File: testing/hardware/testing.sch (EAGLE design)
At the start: 17 parts

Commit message: CAM files for PCB
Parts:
- J1: value (none) -> SPI_COMM
- X1: value (none) -> POWER
- X2: value (none) -> CAN_HI_LO
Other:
- note added: "CAN Bus Testing Module"
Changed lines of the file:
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@@
 </variantdefs>
 <classes>
-<class number="0" name="default" width="0.3048" drill="0.508">
+<class number="0" name="default" width="0.762" drill="0.508">
 <clearance class="0" value="0.3048"/>
+</class>
+<class number="1" name="power" width="1.27" drill="0.508">
+<clearance class="1" value="0.508"/>
 </class>
 </classes>
@@
 <part name="P+5" library="SparkFun" deviceset="VCC" device=""/>
 <part name="GND4" library="SparkFun" deviceset="GND" device=""/>
-<part name="X1" library="con-wago-500" deviceset="W237-102" device=""/>
-<part name="X2" library="con-wago-500" deviceset="W237-102" device=""/>
-<part name="J1" library="con-amp" deviceset="MTA05-156" device=""/>
-<part name="FRAME1" library="frames" library_urn="urn:adsk.eagle:library:229" deviceset="FRAME_A_L" device=""/>
+<part name="X1" library="con-wago-500" deviceset="W237-102" device="" value="POWER"/>
+<part name="X2" library="con-wago-500" deviceset="W237-102" device="" value="CAN_HI_LO"/>
+<part name="J1" library="con-amp" deviceset="MTA05-156" device="" value="SPI_COMM"/>
+<part name="FRAME1" library="frames" library_urn="urn:adsk.eagle:library:229" deviceset="FRAME_A_L" device="" value="frame"/>
 </parts>
 <sheets>
 <sheet>
 <plain>
+<text x="185.42" y="25.4" size="2.54" layer="94">CAN Bus Testing Module </text>
 </plain>
 <instances>
@@
 </instance>
 <instance part="X2" gate="-2" x="254" y="121.92" smashed="yes" rot="R180">
-<attribute name="VALUE" x="256.54" y="125.603" size="1.778" layer="96" rot="R180"/>
+<attribute name="VALUE" x="254" y="117.983" size="1.778" layer="96" rot="R180"/>
 <attribute name="NAME" x="254" y="121.031" size="1.778" layer="95"/>
 </instance>
@@
 </segment>
 </net>
-<net name="GND" class="0">
+<net name="GND" class="1">
 <segment>
 <pinref part="GND" gate="1" pin="GND"/>
@@
 <wire x1="81.28" y1="99.06" x2="71.12" y2="99.06" width="0.1524" layer="91"/>
 <wire x1="71.12" y1="99.06" x2="71.12" y2="96.52" width="0.1524" layer="91"/>
-<wire x1="20.32" y1="116.84" x2="22.86" y2="116.84" width="0.1524" layer="91"/>
-<wire x1="22.86" y1="116.84" x2="81.28" y2="116.84" width="0.1524" layer="91"/>
 <wire x1="81.28" y1="116.84" x2="81.28" y2="99.06" width="0.1524" layer="91"/>
 <junction x="81.28" y="99.06"/>
 <pinref part="X1" gate="-2" pin="KL"/>
+<wire x1="20.32" y1="116.84" x2="22.86" y2="116.84" width="0.1524" layer="91"/>
+<wire x1="22.86" y1="116.84" x2="81.28" y2="116.84" width="0.1524" layer="91"/>
 <junction x="22.86" y="116.84"/>
 </segment>
@@
 </segment>
 </net>
-<net name="VCC" class="0">
+<net name="VCC" class="1">
 <segment>
 <pinref part="R1" gate="G$1" pin="2"/>
@@
 </sheet>
 </sheets>
+<errors>
+</errors>
 </schematic>
 </drawing>

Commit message: test module updates
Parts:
- added LED4, LED5: (no value), adafruit:LED5MM
- added R7, R8: 220 Ω, adafruit:R-US_0204/7
- added X3: TEST_LED, con-wago-500:W237-102
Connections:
- net N$1 renamed RXCAN
- net N$10 renamed CS
- net N$11 renamed SCK
- net N$12 renamed CAN_H
- net N$14 renamed SI
- net N$15 renamed SO
- net N$17 renamed CAN_L
- net N$2 renamed TXCAN
- net N$7 renamed INT
- new net N$1: R7.2, X3-2.KL
- new net N$10: LED5.A, R8.1
- new net N$2: R8.2, X3-1.KL
- new net N$7: LED4.A, R7.1
- net GND: now also LED4.C, LED5.C
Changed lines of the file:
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@@
 <part name="J1" library="con-amp" deviceset="MTA05-156" device="" value="SPI_COMM"/>
 <part name="FRAME1" library="frames" library_urn="urn:adsk.eagle:library:229" deviceset="FRAME_A_L" device="" value="frame"/>
+<part name="LED4" library="adafruit" deviceset="LED" device="5MM"/>
+<part name="R7" library="adafruit" deviceset="R-US_" device="0204/7" value="220 Ω"/>
+<part name="LED5" library="adafruit" deviceset="LED" device="5MM"/>
+<part name="R8" library="adafruit" deviceset="R-US_" device="0204/7" value="220 Ω"/>
+<part name="GND5" library="SparkFun" deviceset="GND" device=""/>
+<part name="GND6" library="SparkFun" deviceset="GND" device=""/>
+<part name="X3" library="con-wago-500" deviceset="W237-102" device="" value="TEST_LED"/>
 </parts>
 <sheets>
@@
 <attribute name="DRAWING_NAME" x="185.42" y="19.05" size="2.54" layer="94"/>
 </instance>
+<instance part="LED4" gate="G$1" x="203.2" y="78.74" smashed="yes">
+<attribute name="NAME" x="206.756" y="74.168" size="1.778" layer="95" rot="R90"/>
+<attribute name="VALUE" x="208.915" y="74.168" size="1.778" layer="96" rot="R90"/>
+</instance>
+<instance part="R7" gate="G$1" x="203.2" y="91.44" smashed="yes" rot="R90">
+<attribute name="NAME" x="201.7014" y="87.63" size="1.778" layer="95" rot="R90"/>
+<attribute name="VALUE" x="206.502" y="87.63" size="1.778" layer="96" rot="R90"/>
+</instance>
+<instance part="LED5" gate="G$1" x="220.98" y="78.74" smashed="yes">
+<attribute name="NAME" x="224.536" y="74.168" size="1.778" layer="95" rot="R90"/>
+<attribute name="VALUE" x="226.695" y="74.168" size="1.778" layer="96" rot="R90"/>
+</instance>
+<instance part="R8" gate="G$1" x="220.98" y="91.44" smashed="yes" rot="R90">
+<attribute name="NAME" x="219.4814" y="87.63" size="1.778" layer="95" rot="R90"/>
+<attribute name="VALUE" x="224.282" y="87.63" size="1.778" layer="96" rot="R90"/>
+</instance>
+<instance part="GND5" gate="1" x="203.2" y="63.5" smashed="yes">
+<attribute name="VALUE" x="200.66" y="60.96" size="1.778" layer="96"/>
+</instance>
+<instance part="GND6" gate="1" x="220.98" y="63.5" smashed="yes">
+<attribute name="VALUE" x="218.44" y="60.96" size="1.778" layer="96"/>
+</instance>
+<instance part="X3" gate="-1" x="246.38" y="99.06" smashed="yes" rot="R180">
+<attribute name="NAME" x="246.38" y="98.171" size="1.778" layer="95"/>
+</instance>
+<instance part="X3" gate="-2" x="246.38" y="104.14" smashed="yes" rot="R180">
+<attribute name="VALUE" x="241.3" y="92.837" size="1.778" layer="96"/>
+<attribute name="NAME" x="246.38" y="103.251" size="1.778" layer="95"/>
+</instance>
 </instances>
 <busses>
 </busses>
 <nets>
-<net name="N$2" class="0">
+<net name="TXCAN" class="0">
 <segment>
 <pinref part="CAN_CONTRL" gate="A" pin="TXCAN"/>
@@
 </segment>
 </net>
-<net name="N$1" class="0">
+<net name="RXCAN" class="0">
 <segment>
 <pinref part="CAN_CONTRL" gate="A" pin="RXCAN"/>
@@
 <wire x1="162.56" y1="144.78" x2="157.48" y2="144.78" width="0.1524" layer="91"/>
 <wire x1="157.48" y1="144.78" x2="157.48" y2="139.7" width="0.1524" layer="91"/>
+</segment>
+<segment>
+<pinref part="LED4" gate="G$1" pin="C"/>
+<wire x1="203.2" y1="73.66" x2="203.2" y2="66.04" width="0.1524" layer="91"/>
+<pinref part="GND5" gate="1" pin="GND"/>
+</segment>
+<segment>
+<pinref part="LED5" gate="G$1" pin="C"/>
+<wire x1="220.98" y1="73.66" x2="220.98" y2="66.04" width="0.1524" layer="91"/>
+<pinref part="GND6" gate="1" pin="GND"/>
 </segment>
 </net>
@@
 </segment>
 </net>
-<net name="N$7" class="0">
+<net name="INT" class="0">
 <segment>
 <pinref part="LED1" gate="G$1" pin="C"/>
@@
 </segment>
 </net>
-<net name="N$12" class="0">
+<net name="CAN_H" class="0">
 <segment>
 <pinref part="CAN_TRANS" gate="A" pin="CANH"/>
@@
 </segment>
 </net>
-<net name="N$17" class="0">
+<net name="CAN_L" class="0">
 <segment>
 <wire x1="251.46" y1="132.08" x2="248.92" y2="132.08" width="0.1524" layer="91"/>
@@
 <junction x="248.92" y="132.08"/>
 <junction x="236.22" y="132.08"/>
-</segment>
-</net>
-<net name="N$11" class="0">
+<wire x1="251.46" y1="132.08" x2="248.92" y2="132.08" width="0.1524" layer="91"/>
+</segment>
+</net>
+<net name="SCK" class="0">
 <segment>
 <pinref part="CAN_CONTRL" gate="A" pin="SCK"/>
@@
 </segment>
 </net>
-<net name="N$14" class="0">
+<net name="SI" class="0">
 <segment>
 <pinref part="J1" gate="G$1" pin="2"/>
@@
 </segment>
 </net>
-<net name="N$15" class="0">
+<net name="SO" class="0">
 <segment>
 <pinref part="J1" gate="G$1" pin="3"/>
@@
 </segment>
 </net>
-<net name="N$10" class="0">
+<net name="CS" class="0">
 <segment>
 <pinref part="CAN_CONTRL" gate="A" pin="~CS"/>
@@
 </segment>
 </net>
+<net name="N$1" class="0">
+<segment>
+<pinref part="R7" gate="G$1" pin="2"/>
+<wire x1="203.2" y1="96.52" x2="203.2" y2="104.14" width="0.1524" layer="91"/>
+<wire x1="203.2" y1="104.14" x2="241.3" y2="104.14" width="0.1524" layer="91"/>
+<pinref part="X3" gate="-2" pin="KL"/>
+</segment>
+</net>
+<net name="N$2" class="0">
+<segment>
+<pinref part="R8" gate="G$1" pin="2"/>
+<wire x1="220.98" y1="96.52" x2="220.98" y2="99.06" width="0.1524" layer="91"/>
+<wire x1="220.98" y1="99.06" x2="241.3" y2="99.06" width="0.1524" layer="91"/>
+<pinref part="X3" gate="-1" pin="KL"/>
+</segment>
+</net>
+<net name="N$7" class="0">
+<segment>
+<pinref part="R7" gate="G$1" pin="1"/>
+<pinref part="LED4" gate="G$1" pin="A"/>
+<wire x1="203.2" y1="86.36" x2="203.2" y2="81.28" width="0.1524" layer="91"/>
+</segment>
+</net>
+<net name="N$10" class="0">
+<segment>
+<pinref part="R8" gate="G$1" pin="1"/>
+<pinref part="LED5" gate="G$1" pin="A"/>
+<wire x1="220.98" y1="86.36" x2="220.98" y2="81.28" width="0.1524" layer="91"/>
+</segment>
+</net>

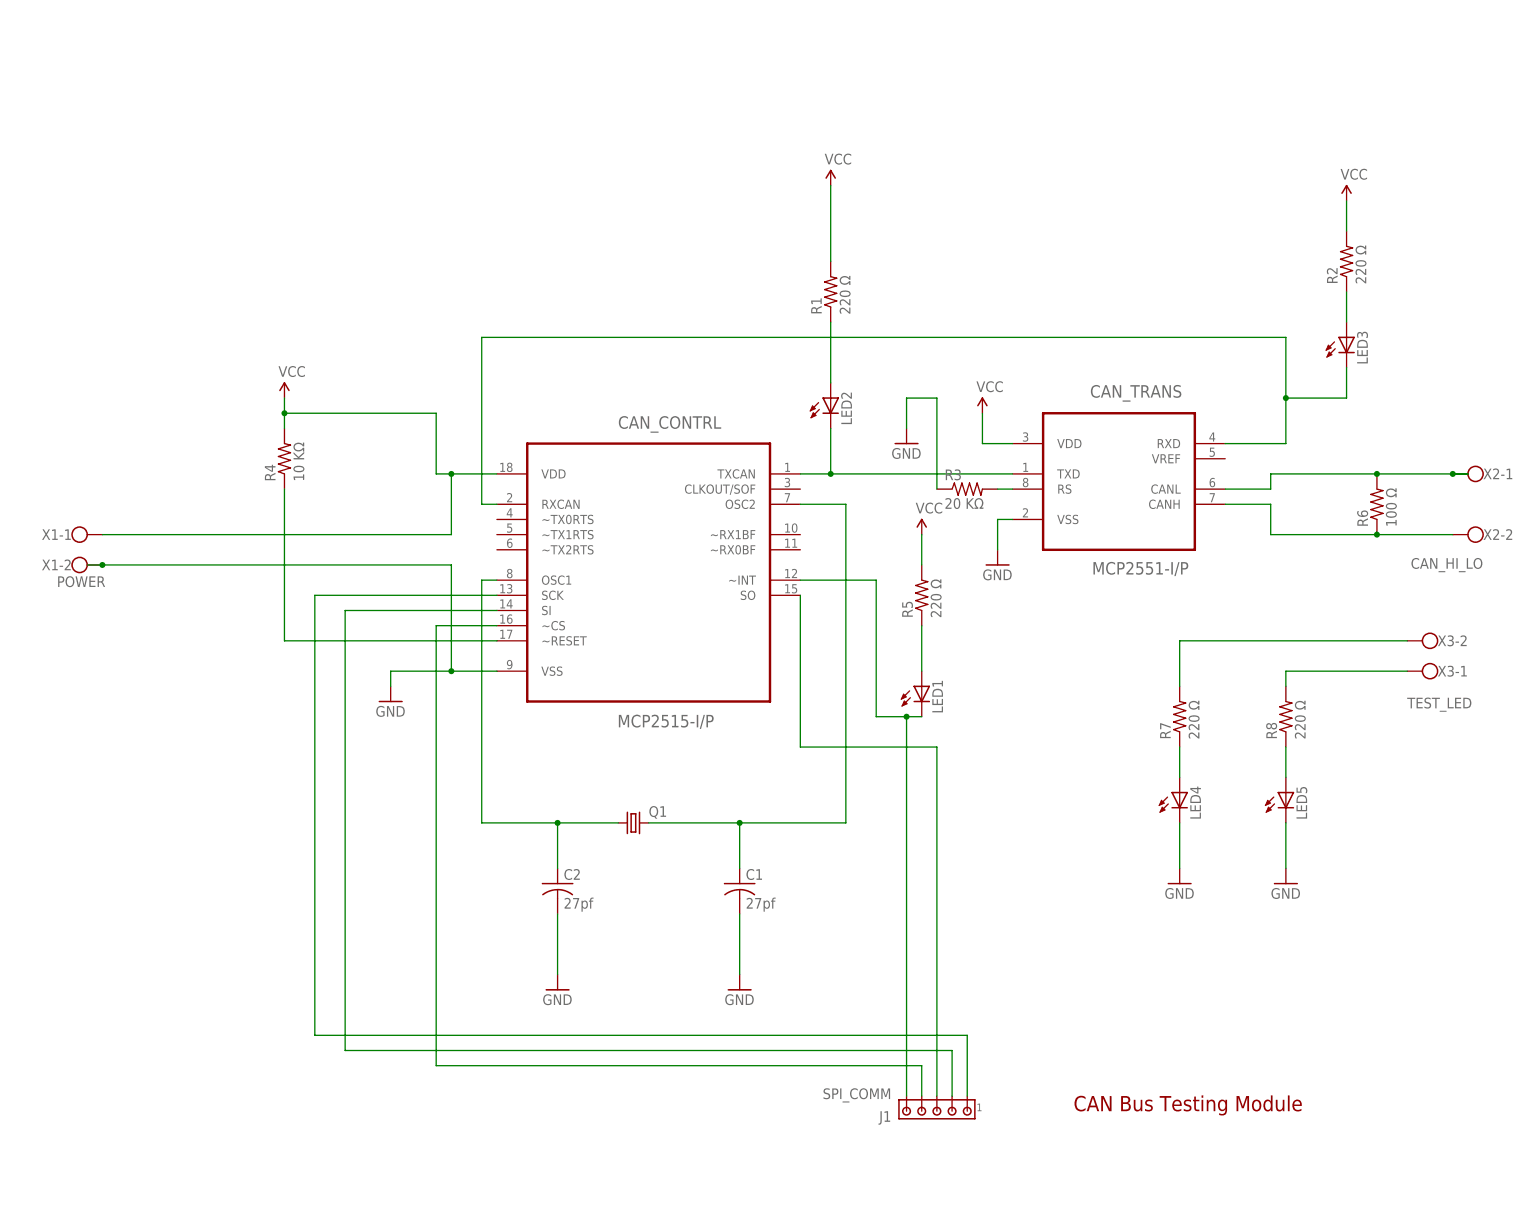
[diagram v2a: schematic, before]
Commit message: android app plus updated board
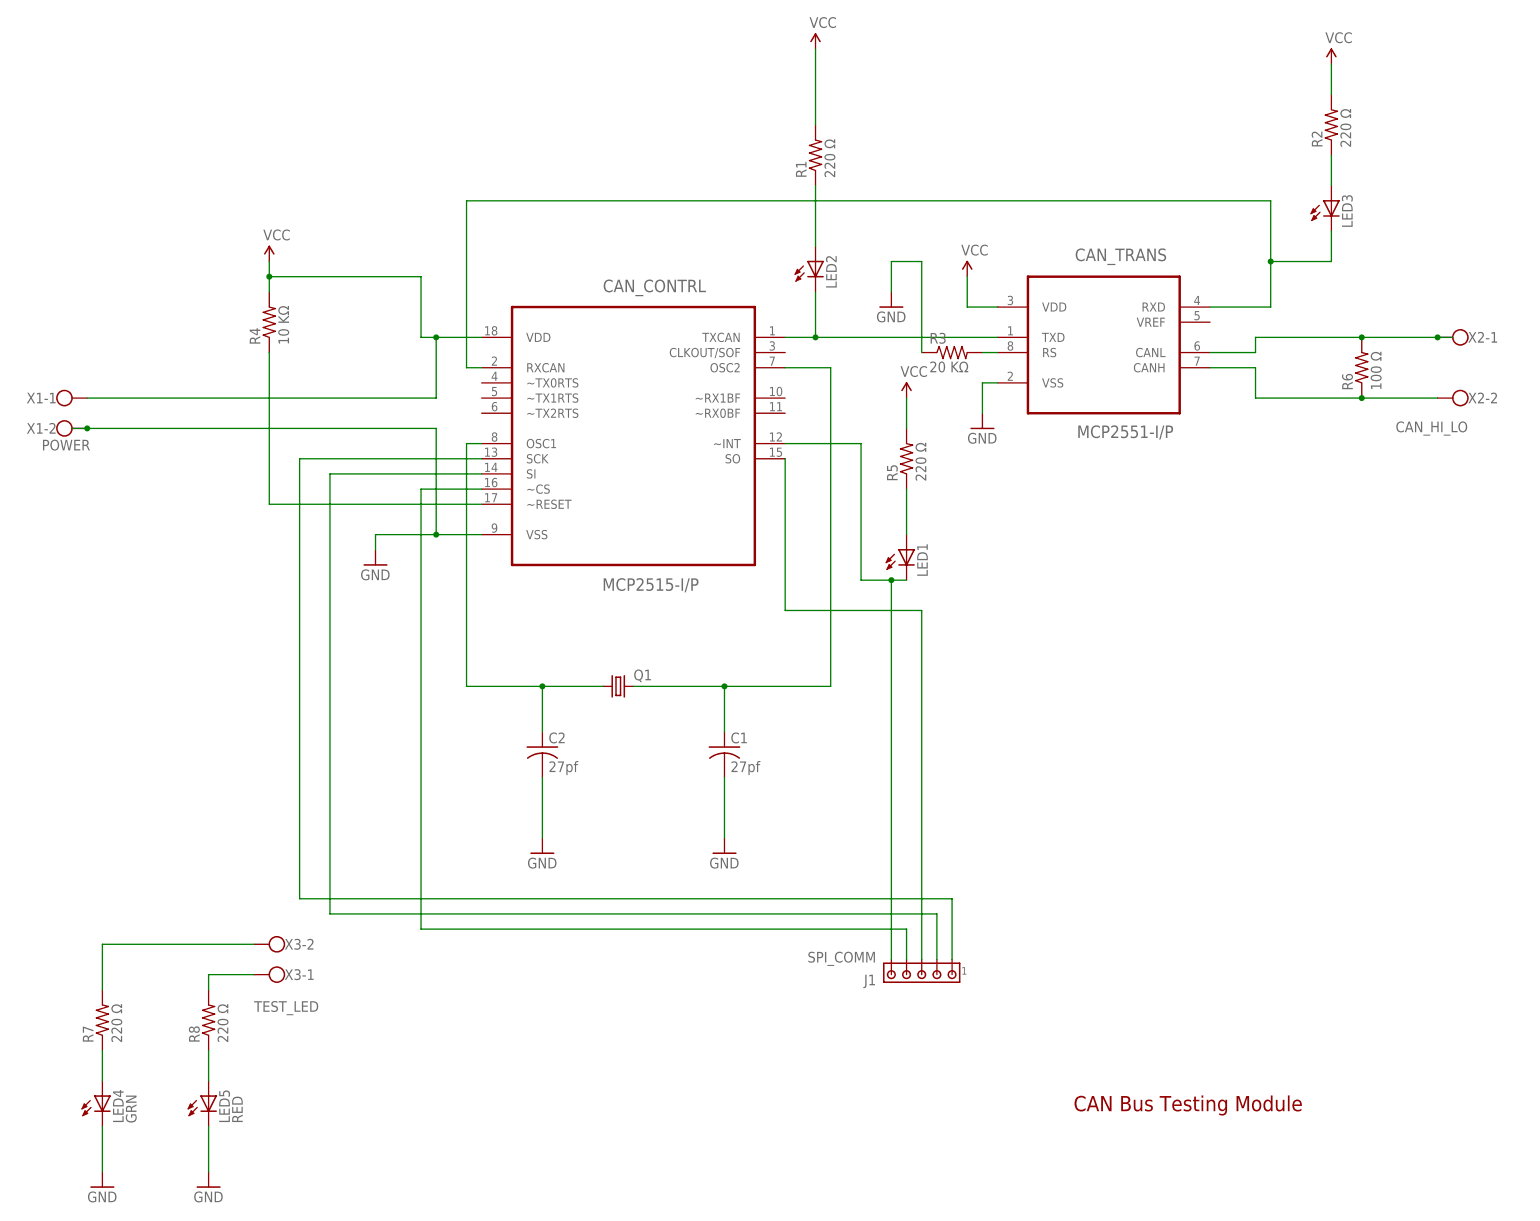
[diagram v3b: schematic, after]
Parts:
- LED4: value (none) -> GRN
- LED5: value (none) -> RED
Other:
- moved on the sheet: C1, C2, CAN_CONTRL, CAN_TRANS, J1, LED1, LED2, LED3, LED4, LED5, Q1, R1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

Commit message: future design schematic and layout
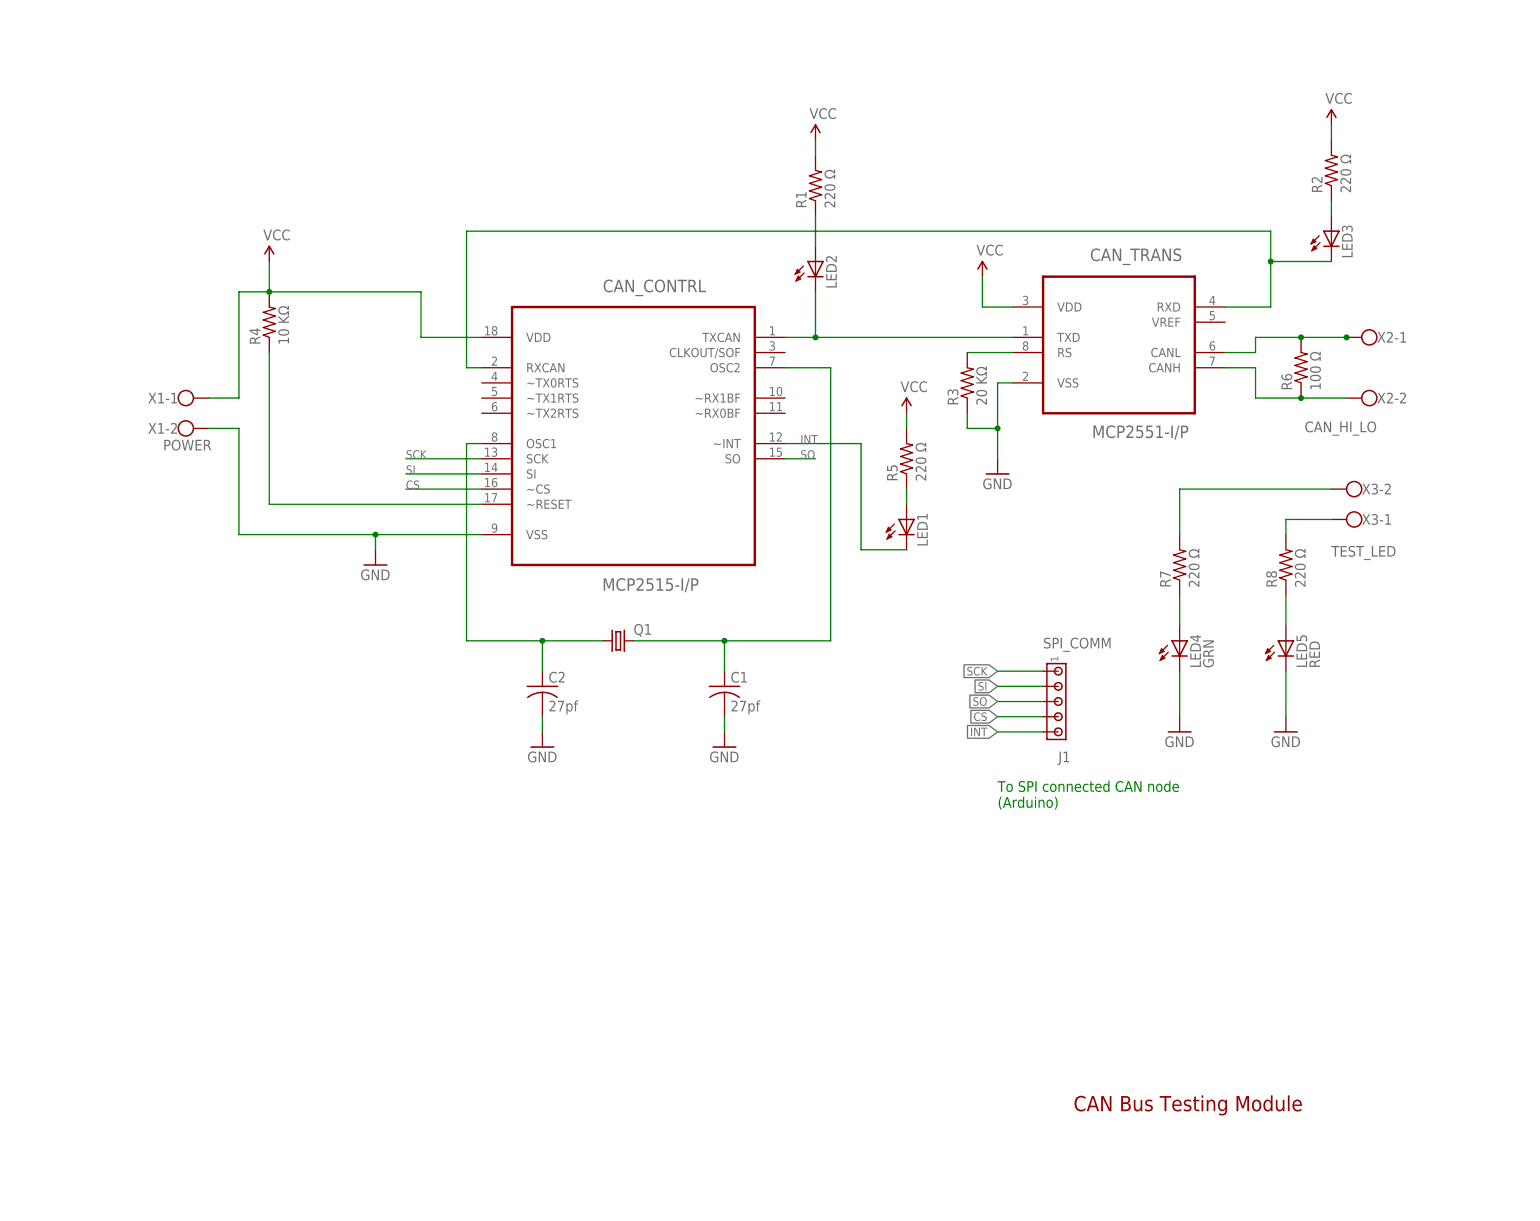
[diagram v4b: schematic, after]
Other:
- note added: "To SPI connected CAN node (Arduino)"
- moved on the sheet: C1, C2, CAN_TRANS, J1, LED1, LED3, LED4, LED5, Q1, R1, R2, R3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

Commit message: all software working on raspberry pi 3b
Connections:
- net N$8 renamed RESET
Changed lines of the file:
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@@
 </segment>
 </net>
-<net name="N$8" class="0">
+<net name="RESET" class="0">
 <segment>
 <pinref part="CAN_CONTRL" gate="A" pin="~RESET"/>
@@
 <wire x1="86.36" y1="127" x2="50.8" y2="127" width="0.1524" layer="91"/>
 <wire x1="50.8" y1="127" x2="50.8" y2="152.4" width="0.1524" layer="91"/>
+<label x="73.66" y="127" size="1.778" layer="95"/>
 </segment>
 </net>

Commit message: minor schematic tweaks
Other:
- moved on the sheet: C1, C2, CAN_CONTRL, CAN_TRANS, J1, LED1, LED2, LED3, LED4, LED5, Q1, R1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
